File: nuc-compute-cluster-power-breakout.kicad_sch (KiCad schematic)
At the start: 60 parts, among them J10 10107844-002LF, J2 BM04B-SRSS-TB-LF-SN, J3 BM04B-SRSS-TB-LF-SN, J4 39288080, J5 39288080, J6 39288080, J7 39288080, J8 39288080, Q11 BC856,215

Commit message: Loclib
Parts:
- R11, R12, R51, R52, R53: footprint antmicro-footprints:0603-res -> nuc-compute-cluster-power-breakout-footprints:0603-res; symbol antmicroResistors0603:R_4k7_0603 -> nuc-compute-cluster-power-breakout:R_4k7_0603
- R54, R55: footprint antmicro-footprints:0603-res -> nuc-compute-cluster-power-breakout-footprints:0603-res; symbol antmicroResistors0603:R_1k_0603 -> nuc-compute-cluster-power-breakout:R_1k_0603
- R56: footprint antmicro-footprints:0603-res -> nuc-compute-cluster-power-breakout-footprints:0603-res; symbol antmicroResistors0603:R_2k2_0603 -> nuc-compute-cluster-power-breakout:R_2k2_0603

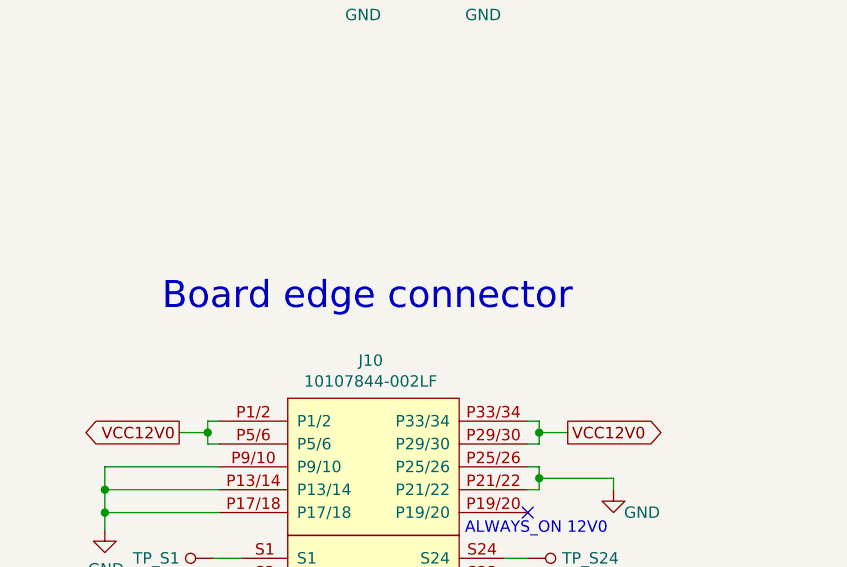
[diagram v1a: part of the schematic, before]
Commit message: Add photo, unify the size of schematic sheets
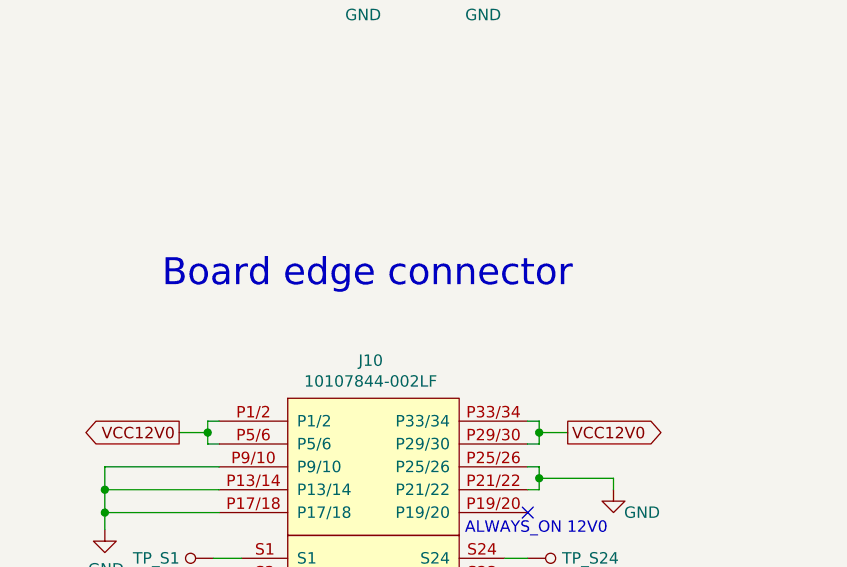
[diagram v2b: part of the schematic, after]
